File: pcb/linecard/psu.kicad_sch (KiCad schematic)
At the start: 85 parts, among them J1 CONN_ATX12V, J2 CONN_01X03, J3 CORTEX_DEBUG_ETM, J4 0532611071, SW1 SWITCH, SW2 SWITCH, U1 MYMGK00504ERSR, U2 MYMGK00504ERSR, U3 MYMGK00504ERSR, U4 MYMGK00504ERSR, U5 STM32L431-QFN48, U6 INA230, U7 INA230, U8 INA230, U9 INA230

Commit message: Hopefully finished first PHY
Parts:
- removed J2: CONN_01X03, azonenberg_pcb:CONN_HEADER_2.54MM_1x3, symbol conn:CONN_01X03
- added R28, R29, R30: R, symbol device:R
- added R64, R65, R66, R67: 1K, symbol device:R
- added TP11, TP12, TP13, TP14, TP15: CONN_COAXIAL, symbol conn:CONN_COAXIAL
- added TP5, TP6: CONN_01X03, azonenberg_pcb:CONN_HEADER_2.54MM_1x3, symbol conn:CONN_01X03
- C1, C11, C12, C16, C17, C2, C6, C7: value 22 uF 25V -> C
- C10, C15, C20, C5: value DNP -> C
- C13, C14, C18, C19, C3, C4, C8, C9: value 220 uF -> C
- C21, C24, C25, C26, C27, C28, C29, C30, C31, C32: value 0.47 uF -> C
- C22: value 4.7 uF -> C
- C23: value 0.1 uF -> C
- D1, D2: value GREEN -> LED
- D3: value RED -> LED
- F1: value 2A -> FUSE_PWROUT_2
- FB1: value MI0603J601R-10 -> INDUCTOR_PWROUT
- FB2: renamed from FB?; value TBD -> INDUCTOR_PWROUT
- J4: value 0532611071 -> CONN_01X10
- R1: value 3k -> R
- R10, R6: value 4.99K -> R
- R11, R14, R15, R4, R8: value 0 -> R
- R12, R16, R3, R7: value TBD -> R-4TERM
- R13: value 2.26K -> R
- R17, R27, R5, R9: value 10K -> R
- R18: value DNP -> R
- R19, R20, R26: value 4.7K -> R
- R2: value 160 -> R
- R21, R22, R23: value 1K -> R
- R24, R25: value 33K -> R
- TP1, TP2, TP3, TP4: value TESTPOINT -> CONN_01X01
- TP16: renamed from TP1; value TESTPOINT -> CONN_01X01
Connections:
- net 3V3_SB is gone; now on net 3V3: SW1.2, SW2.2, U5.1 (VBAT), U5.24 (VDD), U5.36 (VDD), U5.48 (VDD)
- net 12V0: now also FB2.1, TP11.1 (In); no longer FB2.2
- net 1V0: now also TP14.1 (In)
- net 1V0_2: now also TP15.1 (In)
- net 2V5: now also R64.2, R65.2, R66.2, R67.2, TP13.1 (In); no longer R16.2 (Vo)
- net 3V3: now also R16.2 (Vo), TP12.1 (In)
- net GND: now also TP11.2 (Ext), TP12.2 (Ext), TP13.2 (Ext), TP14.2 (Ext), TP15.2 (Ext), TP5.3 (P3), TP6.3 (P3)
- net I2C_SCL: now also R29.2, TP6.2 (P2); no longer J4.7 (P7)
- net I2C_SDA: now also R28.2, TP6.1 (P1); no longer J4.6 (P6)
- net SPI_MISO: now also R30.1; no longer U5.16 (PA6)
- net UART_RX: now also TP5.1 (P1)
- net UART_TX: now also TP5.2 (P2)
- net PHY0_PWRDN: now reaches U5.5 (PH0)
- net PHY0_PWRDN: now also R66.1
- net PHY1_PWRDN: now reaches U5.6 (PH1)
- net PHY1_PWRDN: now also R67.1
- net at F1.2: now also FB2.2; no longer FB2.1
- net PHY0_RST: now reaches U5.26 (PB13)
- net PHY0_RST: now also R64.1
- net PHY1_RST: now reaches U5.27 (PB14)
- net PHY1_RST: now also R65.1
- net 3V3_EN: no longer names the net of U5.19 (PB1)
- new net: J4.6 (P6), R28.1
- new net: J4.7 (P7), R29.1
- new net: R30.2, U5.16 (PA6)
- no-connect marks 15 -> 12
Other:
- note added: "PHYx_* outputs are open drain Require external pull to 2V5"
- note added: "Rail test points"
- company: (none) -> Antikernel Labs
- title: (none) -> LATENTRED Line Card
- moved on the sheet: FB2, U5A, U5B

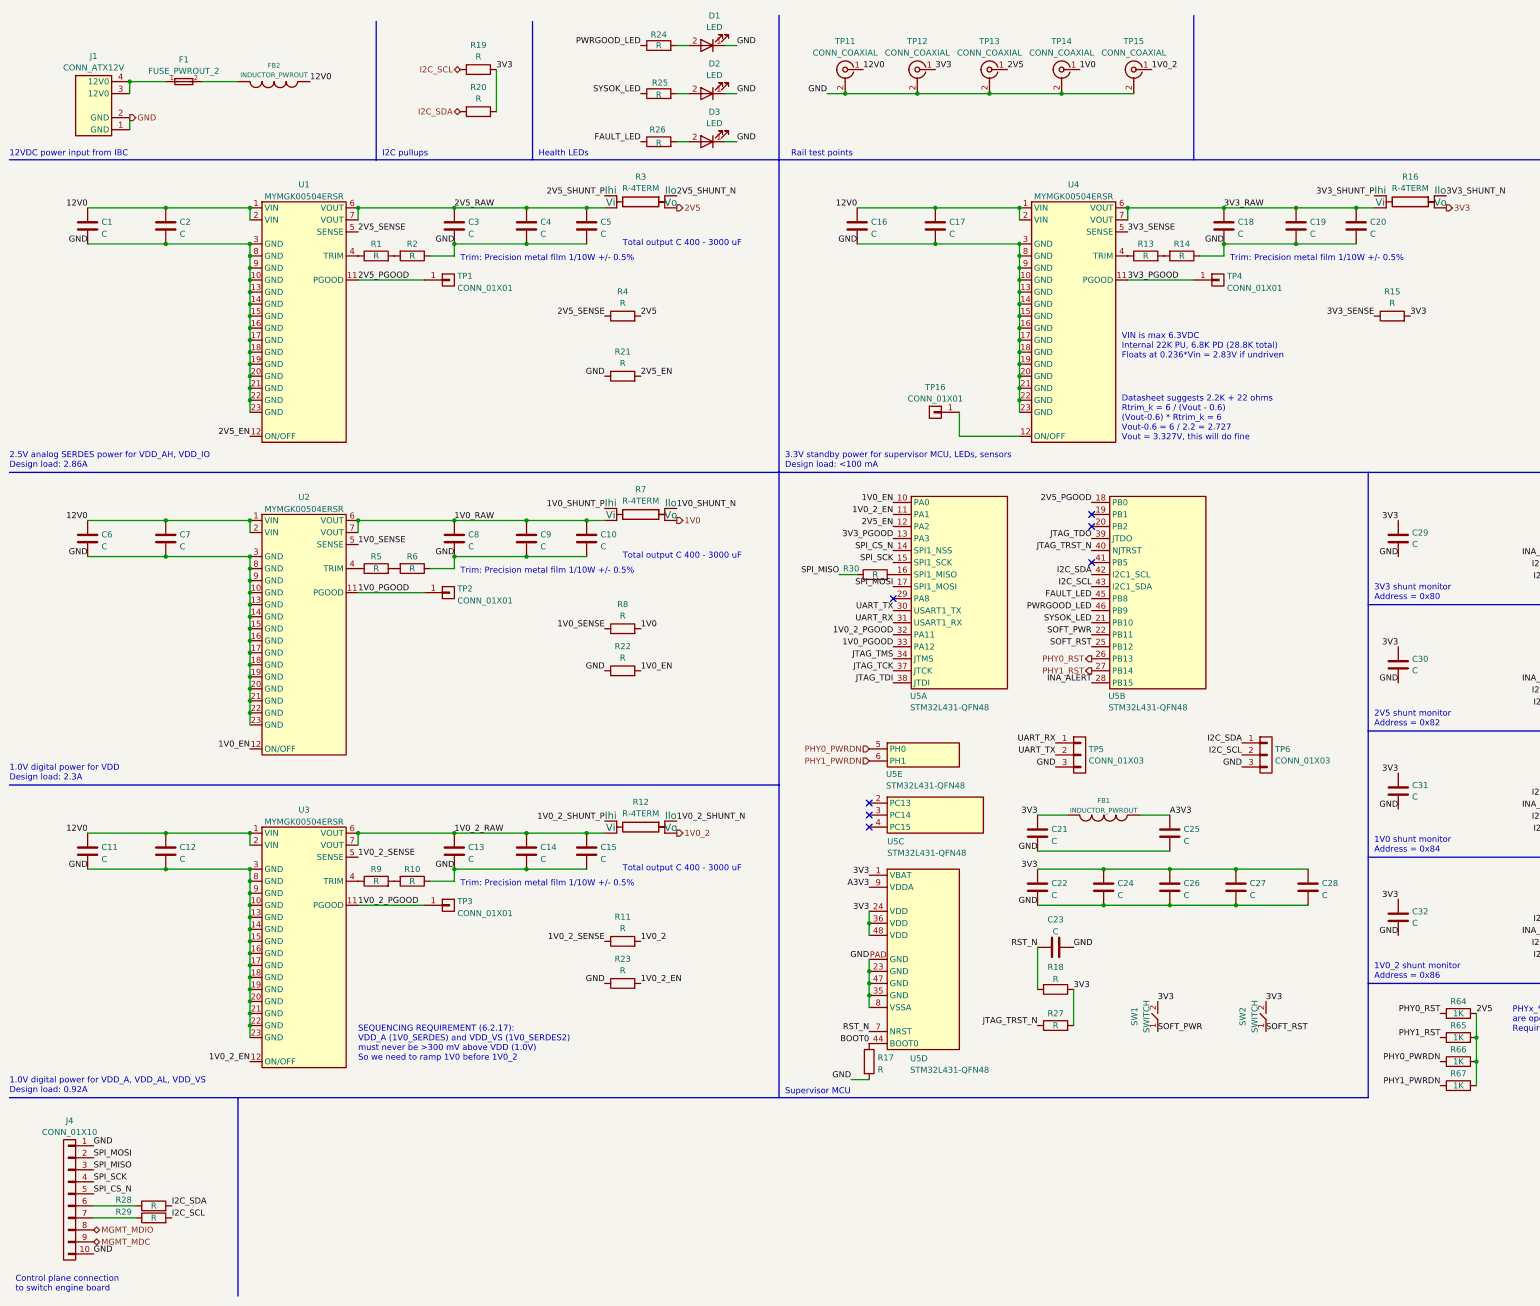
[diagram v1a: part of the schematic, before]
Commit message: Finished initial schematic of line card
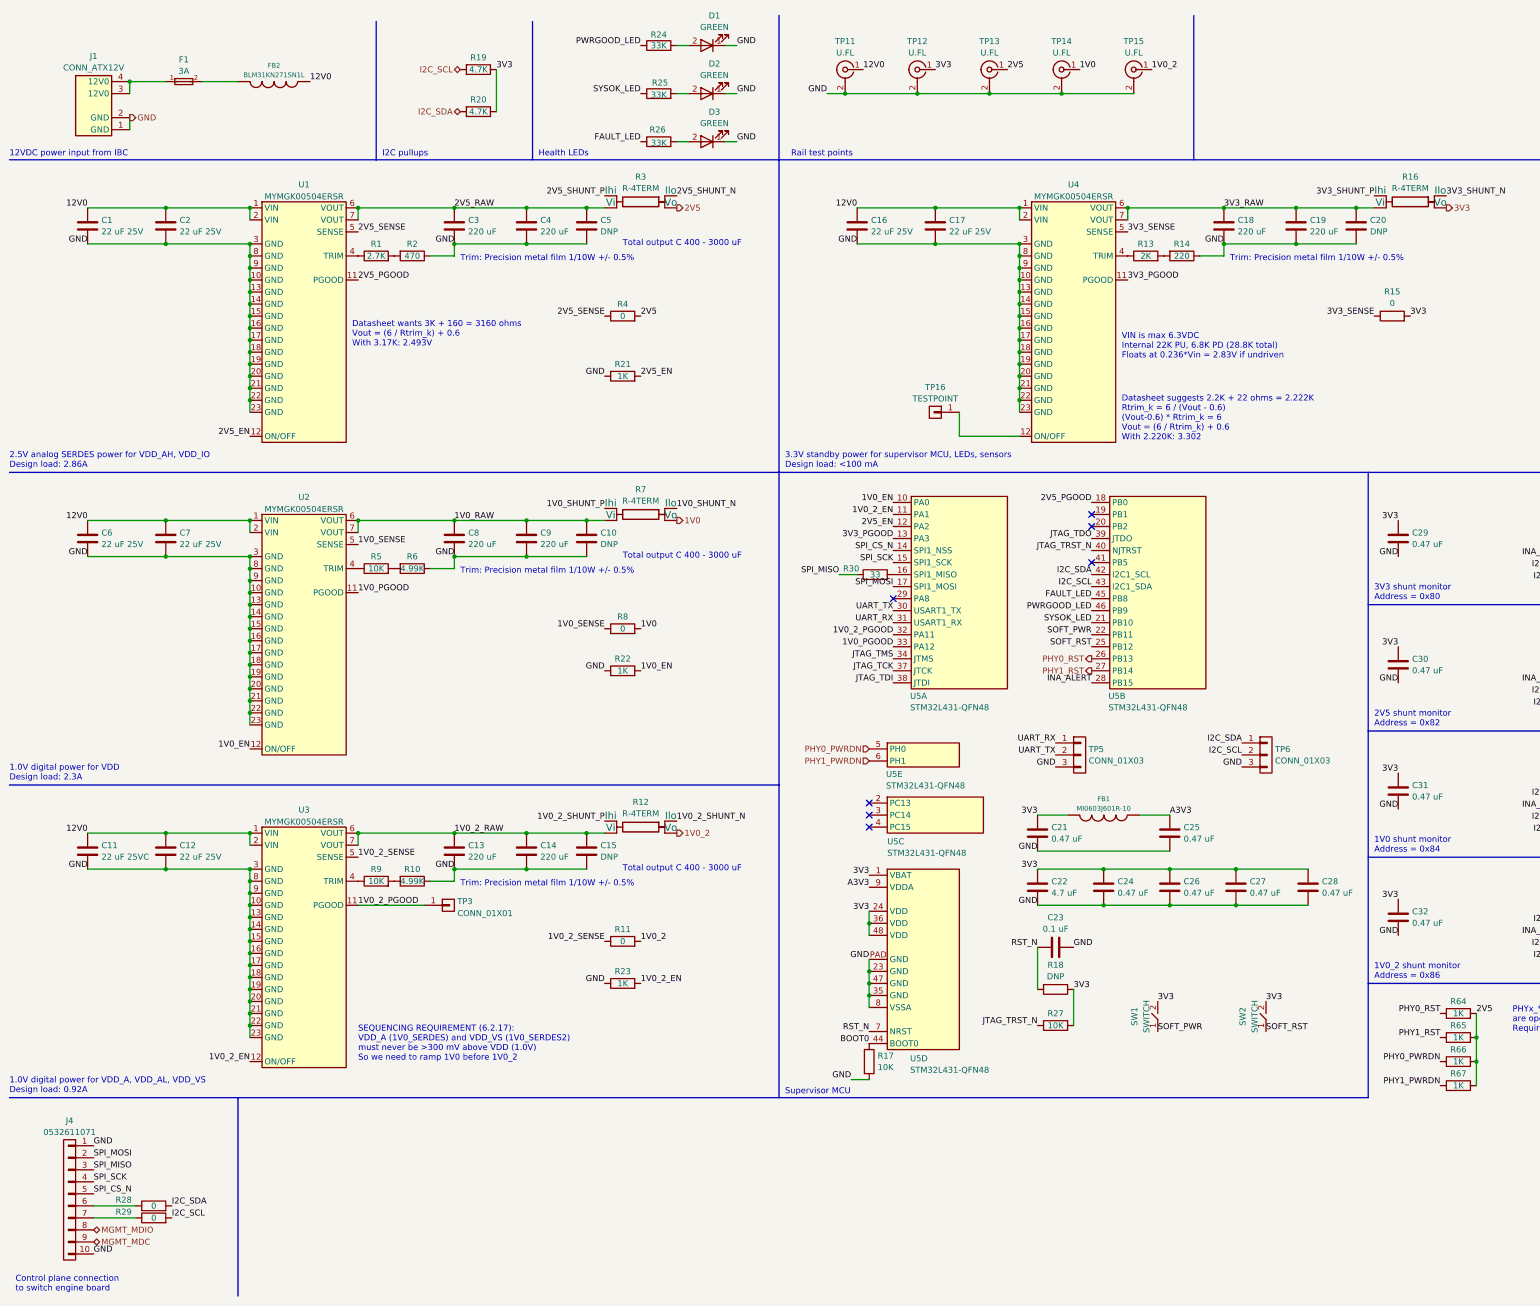
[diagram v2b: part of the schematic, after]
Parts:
- removed TP1, TP2, TP4: CONN_01X01, azonenberg_pcb:TESTPOINT_SMT_0.5MM, symbol conn:CONN_01X01
- C1, C12, C16, C17, C2, C6, C7: value C -> 22 uF 25V
- C10, C15, C20, C5: value C -> DNP
- C11: value C -> 22 uF 25VC
- C13, C14, C18, C19, C3, C4, C8, C9: value C -> 220 uF
- C21, C24, C25, C26, C27, C28: value C -> 0.47 uF
- C22: value C -> 4.7 uF
- C23: value C -> 0.1 uF
- C29, C30, C31, C32: value C -> 0.47 uF; footprint (none) -> azonenberg_pcb:EIA_0402_CAP_NOSILK
- D1, D2, D3: value LED -> GREEN
- F1: value FUSE_PWROUT_2 -> 3A
- FB1: value INDUCTOR_PWROUT -> MI0603J601R-10
- FB2: value INDUCTOR_PWROUT -> BLM31KN271SN1L
- J4: value CONN_01X10 -> 0532611071
- R1: value R -> 2.7K
- R10, R6: value R -> 4.99K
- R11, R15, R28, R29, R4, R8: value R -> 0; footprint (none) -> azonenberg_pcb:EIA_0402_RES_NOSILK
- R13: value R -> 2K
- R14: value R -> 220
- R17, R27, R5, R9: value R -> 10K
- R18: value R -> DNP
- R19, R20: value R -> 4.7K
- R2: value R -> 470
- R21, R22, R23: value R -> 1K; footprint (none) -> azonenberg_pcb:EIA_0402_RES_NOSILK
- R24, R25, R26: value R -> 33K
- R30: value R -> 33; footprint (none) -> azonenberg_pcb:EIA_0402_RES_NOSILK
- R64, R65, R66, R67: footprint (none) -> azonenberg_pcb:EIA_0402_RES_NOSILK
- TP11, TP12, TP13, TP14, TP15: value CONN_COAXIAL -> U.FL; footprint (none) -> azonenberg_pcb:CONN_U.FL_TE_1909763-1
- TP16: value CONN_01X01 -> TESTPOINT; footprint (none) -> azonenberg_pcb:TESTPOINT_SMT_0.5MM
- U6, U7, U8, U9: footprint (none) -> azonenberg_pcb:QFN_16_0.5MM_3x3MM
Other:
- note added: "Datasheet suggests 2.2K + 22 ohms = 2.222K Rtrim_k = 6 / (Vout - 0.6) (Vout-0.6) * Rtrim_k = 6 Vout = (6 / Rtrim_k) + 0.6 With 2.220K: 3.302"
- note added: "Datasheet wants 3K + 160 = 3160 ohms Vout = (6 / Rtrim_k) + 0.6 With 3.17K: 2.493V"
- note removed: "Datasheet suggests 2.2K + 22 ohms Rtrim_k = 6 / (Vout - 0.6) (Vout-0.6) * Rtrim_k = 6 Vout-0.6 = 6 / 2.2 = 2.727 Vout = 3.327V, this will do fine"

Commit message: Added heatsink, some silkscreen logos, mounting holes, and ground clips
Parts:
- added C485, C486, C487: 0.47 uF, azonenberg_pcb:EIA_0402_CAP_NOSILK, symbol device:C
- added U62, U63, U64: AT30TS74_UDFN, symbol special-azonenberg:AT30TS74_UDFN
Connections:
- net 3V3: now also C485.1, C486.1, C487.1, U62.8 (VCC), U63.7 (A0), U63.8 (VCC), U64.6 (A1), U64.8 (VCC)
- net GND: now also C485.2, C486.2, C487.2, U62.4 (GND), U62.5 (A2), U62.6 (A1), U62.7 (A0), U63.4 (GND), U63.5 (A2), U63.6 (A1), U64.4 (GND), U64.5 (A2), U64.7 (A0)
- net I2C_SCL: now also U62.2 (SCL), U63.2 (SCL), U64.2 (SCL)
- net I2C_SDA: now also U62.1 (SDA), U63.1 (SDA), U64.1 (SDA)
- net TEMP_ALERT: now reaches U5.19 (PB1)
- net TEMP_ALERT: now also U62.3 (ALERT), U63.3 (ALERT), U64.3 (ALERT)
- no-connect marks 12 -> 11
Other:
- note added: "Address = 0x90"
- note added: "Address = 0x92"
- note added: "Address = 0x94"
- note added: "PHY 0 temperature sensor"
- note added: "PHY 1 temperature sensor"
- note added: "PSU temperature sensor"
- note added: "Pullups"
- moved on the sheet: R64, R65, R66, R67

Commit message: Finished initial schematic review
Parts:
- added C488: DNP, azonenberg_pcb:CAP_AL_10MM_SMT, symbol device:C
- added R99: 33, azonenberg_pcb:EIA_0402_RES_NOSILK, symbol device:R
- added TP22: CONN_01X03, azonenberg_pcb:CONN_HEADER_2.54MM_1x3, symbol conn:CONN_01X03
- D3: value GREEN -> RED
- F1: footprint (none) -> azonenberg_pcb:EIA_0402_RES_NOSILK
- FB2: footprint (none) -> azonenberg_pcb:EIA_1206_CAP_NOSILK
- J1: footprint (none) -> azonenberg_pcb:CONN_MOLEX_MINIFITJR_4POS_0039291048
- J4: footprint (none) -> azonenberg_pcb:CONN_MOLEX_PICOBLADE_10POS_0532611071
- R12, R16, R3, R7: value R-4TERM -> LVK25R005FER; footprint (none) -> azonenberg_pcb:OHMITE_LVK25
- R26: value 33K -> 4.7K
- U62, U63, U64: footprint (none) -> azonenberg_pcb:DFN_8_0.5MM_2x3MM_TALL
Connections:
- net 12V0: now also C488.1
- net GND: now also C488.2, TP22.3 (P3)
- net JTAG_TDO: now also R99.1; no longer U5.39 (PB3)
- net MGMT_MDC: now also TP22.2 (P2)
- net MGMT_MDIO: now also TP22.1 (P1)
- new net: R99.2, U5.39 (PB3)
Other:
- note added: "MDIO bus test point"
- note added: "NOTE: MDIO/MDC is LVCMOS25 All other signals LVCMOS33"
- note added: "With 5 milliohm shunt, 5 mV/A 2.5 uV/LSB shunt resolution gives 500 uA, should be fine"
- moved on the sheet: U5B

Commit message: Finished routing of left PHY
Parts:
- TP22, TP5, TP6: footprint azonenberg_pcb:CONN_HEADER_2.54MM_1x3 -> azonenberg_pcb:CONN_HEADER_2.54MM_1x3_REFLOW
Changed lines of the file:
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@@
 	(title_block
 		(title "LATENTRED Line Card")
-		(date "2024-12-13")
+		(date "2024-12-14")
 		(rev "0.1")
 		(company "Antikernel Labs")
@@
 			)
 		)
-		(property "Footprint" "azonenberg_pcb:CONN_HEADER_2.54MM_1x3"
+		(property "Footprint" "azonenberg_pcb:CONN_HEADER_2.54MM_1x3_REFLOW"
 			(at 90.17 274.32 0)
 			(effects
@@
 			)
 		)
-		(property "Footprint" "azonenberg_pcb:CONN_HEADER_2.54MM_1x3"
+		(property "Footprint" "azonenberg_pcb:CONN_HEADER_2.54MM_1x3_REFLOW"
 			(at 240.03 168.91 0)
 			(effects
@@
 			)
 		)
-		(property "Footprint" "azonenberg_pcb:CONN_HEADER_2.54MM_1x3"
+		(property "Footprint" "azonenberg_pcb:CONN_HEADER_2.54MM_1x3_REFLOW"
 			(at 279.4 168.91 0)
 			(effects

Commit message: Continued power supply routing
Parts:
- removed TP3: CONN_01X01, azonenberg_pcb:TESTPOINT_SMT_0.5MM, symbol conn:CONN_01X01
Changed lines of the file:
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@@
 	(title_block
 		(title "LATENTRED Line Card")
-		(date "2024-12-15")
+		(date "2024-12-17")
 		(rev "0.1")
 		(company "Antikernel Labs")
@@
 		)
 	)
-	(wire
-		(pts
-			(xy 87.63 200.66) (xy 101.6 200.66)
-		)
-		(stroke
-			(width 0)
-			(type default)
-		)
-	)
 	(polyline
 		(pts
@@
 					(unit 1)
 				)
-			)
-		)
-	)
-	(symbol
-		(lib_id "conn:CONN_01X01")
-		(at 106.68 200.66 0)
-		(unit 1)
-		(exclude_from_sim no)
-		(in_bom yes)
-		(on_board yes)
-		(dnp no)
-		(fields_autoplaced yes)
-		(property "Reference" "TP3"
-			(at 108.585 199.8253 0)
-			(effects
-				(font
-					(size 1.27 1.27)
-				)
-				(justify left)
-			)
-		)
-		(property "Value" "CONN_01X01"
-			(at 108.585 202.3622 0)
-			(effects
-				(font
-					(size 1.27 1.27)
-				)
-				(justify left)
-			)
-		)
-		(property "Footprint" "azonenberg_pcb:TESTPOINT_SMT_0.5MM"
-			(at 106.68 200.66 0)
-			(effects
-				(font
-					(size 1.27 1.27)
-				)
-				(hide yes)
-			)
-		)
-		(property "Datasheet" ""
-			(at 106.68 200.66 0)
-			(effects
-				(font
-					(size 1.27 1.27)
-				)
-				(hide yes)
-			)
-		)
-		(property "Description" "Connector, single row, 01x01, pin header"
-			(at 106.68 200.66 0)
-			(effects
-				(font
-					(size 1.27 1.27)
-				)
-				(hide yes)
-			)
-		)
-		(pin "1"
-		)
-		(instances
-			(project "linecard"
-				(path "/a55ad1ec-4cad-4d06-8b73-31c98dcc1d79/469d62e1-ca98-4f55-b49b-af1151f42c56"
-					(reference "TP3")
-					(unit 1)
-				)
